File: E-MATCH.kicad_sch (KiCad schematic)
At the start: 7 parts, among them IC1 NCV81071BZR2G, J1 Screw_Terminal_01x02, Q1 IRF3205, U1 TMCS1108A2UQDR

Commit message: Updating Schematic Test
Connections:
- net 3V3 is gone; now on net 5V: U1.8 (VS)
- net Sensor_Output: now reaches U1.7 (VOUT)
- net Sensor_Output: now also A1.19 (A0)
- net 5V: now reaches A1.27 (+5V)
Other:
- moved on the sheet: D1
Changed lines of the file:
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@@
 	)
 	(junction
-		(at 45.72 102.87)
+		(at 45.72 85.09)
 		(diameter 0)
 		(color 0 0 0 0)
 	)
 	(junction
-		(at 45.72 88.9)
+		(at 45.72 95.25)
 		(diameter 0)
 		(color 0 0 0 0)
@@
 	(wire
 		(pts
-			(xy 45.72 102.87) (xy 45.72 119.38)
+			(xy 172.72 62.23) (xy 177.8 62.23)
+		)
+		(stroke
+			(width 0)
+			(type default)
+		)
+	)
+	(wire
+		(pts
+			(xy 45.72 91.44) (xy 45.72 95.25)
 		)
 		(stroke
@@
 	(wire
 		(pts
+			(xy 45.72 85.09) (xy 45.72 88.9)
+		)
+		(stroke
+			(width 0)
+			(type default)
+		)
+	)
+	(wire
+		(pts
 			(xy 95.25 60.96) (xy 95.25 67.31)
 		)
@@
 	(wire
 		(pts
-			(xy 45.72 88.9) (xy 45.72 59.69)
+			(xy 45.72 59.69) (xy 45.72 85.09)
 		)
 		(stroke
@@
 	(wire
 		(pts
+			(xy 165.1 35.56) (xy 165.1 36.83)
+		)
+		(stroke
+			(width 0)
+			(type default)
+		)
+	)
+	(wire
+		(pts
 			(xy 50.8 59.69) (xy 50.8 58.42)
 		)
@@
 	(wire
 		(pts
-			(xy 45.72 102.87) (xy 74.93 102.87)
-		)
-		(stroke
-			(width 0)
-			(type default)
-		)
-	)
-	(wire
-		(pts
-			(xy 74.93 88.9) (xy 74.93 93.98)
-		)
-		(stroke
-			(width 0)
-			(type default)
-		)
-	)
-	(wire
-		(pts
 			(xy 160.02 87.63) (xy 160.02 90.17)
 		)
@@
 	(wire
 		(pts
+			(xy 88.9 50.8) (xy 91.44 50.8)
+		)
+		(stroke
+			(width 0)
+			(type default)
+		)
+	)
+	(wire
+		(pts
+			(xy 45.72 95.25) (xy 45.72 119.38)
+		)
+		(stroke
+			(width 0)
+			(type default)
+		)
+	)
+	(wire
+		(pts
 			(xy 53.34 45.72) (xy 49.53 45.72)
 		)
@@
 	(wire
 		(pts
-			(xy 45.72 91.44) (xy 45.72 102.87)
-		)
-		(stroke
-			(width 0)
-			(type default)
-		)
-	)
-	(wire
-		(pts
 			(xy 45.72 46.99) (xy 49.53 46.99)
 		)
@@
 	(wire
 		(pts
-			(xy 45.72 88.9) (xy 74.93 88.9)
-		)
-		(stroke
-			(width 0)
-			(type default)
-		)
-	)
-	(wire
-		(pts
 			(xy 50.8 59.69) (xy 50.8 60.96)
 		)
@@
 	(wire
 		(pts
+			(xy 45.72 95.25) (xy 57.15 95.25)
+		)
+		(stroke
+			(width 0)
+			(type default)
+		)
+	)
+	(wire
+		(pts
 			(xy 140.97 128.27) (xy 148.59 128.27)
 		)
@@
 	(wire
 		(pts
-			(xy 74.93 102.87) (xy 74.93 104.14)
+			(xy 57.15 85.09) (xy 45.72 85.09)
 		)
 		(stroke
@@
 		)
 	)
-	(global_label "3V3"
+	(global_label "5V"
 		(shape input)
 		(at 93.98 45.72 0)
@@
 		)
 		(property "Intersheetrefs" "${INTERSHEET_REFS}"
-			(at 100.4728 45.72 0)
+			(at 99.2633 45.72 0)
+			(effects
+				(font
+					(size 1.27 1.27)
+				)
+				(justify left)
+				(hide yes)
+			)
+		)
+	)
+	(global_label "5V"
+		(shape input)
+		(at 165.1 35.56 90)
+		(fields_autoplaced yes)
+		(effects
+			(font
+				(size 1.27 1.27)
+			)
+			(justify left)
+		)
+		(property "Intersheetrefs" "${INTERSHEET_REFS}"
+			(at 165.1 30.2767 90)
+			(effects
+				(font
+					(size 1.27 1.27)
+				)
+				(justify left)
+				(hide yes)
+			)
+		)
+	)
+	(global_label "Sensor_Output"
+		(shape input)
+		(at 91.44 50.8 0)
+		(fields_autoplaced yes)
+		(effects
+			(font
+				(size 1.27 1.27)
+			)
+			(justify left)
+		)
+		(property "Intersheetrefs" "${INTERSHEET_REFS}"
+			(at 108.0321 50.8 0)
 			(effects
 				(font
@@
 		(property "Intersheetrefs" "${INTERSHEET_REFS}"
 			(at 53.12 36.83 0)
+			(effects
+				(font
+					(size 1.27 1.27)
+				)
+				(justify left)
+				(hide yes)
+			)
+		)
+	)
+	(global_label "Sensor_Output"
+		(shape input)
+		(at 177.8 62.23 0)
+		(fields_autoplaced yes)
+		(effects
+			(font
+				(size 1.27 1.27)
+			)
+			(justify left)
+		)
+		(property "Intersheetrefs" "${INTERSHEET_REFS}"
+			(at 194.3921 62.23 0)
 			(effects
 				(font
@@
 	(symbol
 		(lib_id "Schottky Diode:MBRS540T3G")
-		(at 74.93 99.06 90)
+		(at 57.15 90.17 90)
 		(unit 1)
 		(exclude_from_sim no)
@@
 		(fields_autoplaced yes)
 		(property "Reference" "D1"
-			(at 77.47 97.7899 90)
+			(at 59.69 88.8999 90)
 			(effects
 				(font
@@
 		)
 		(property "Value" "MBRS540T3G"
-			(at 77.47 100.3299 90)
+			(at 59.69 91.4399 90)
 			(effects
 				(font
@@
 		)
 		(property "Footprint" "Schottky Diode:DIOM7959X261N"
-			(at 74.93 99.06 0)
+			(at 57.15 90.17 0)
 			(effects
 				(font
@@
 		)
 		(property "Datasheet" ""
-			(at 74.93 99.06 0)
+			(at 57.15 90.17 0)
 			(effects
 				(font
@@
 		)
 		(property "Description" ""
-			(at 74.93 99.06 0)
+			(at 57.15 90.17 0)
 			(effects
 				(font
@@
 		)
 		(property "PARTREV" "7/27/2017"
-			(at 74.93 99.06 0)
+			(at 57.15 90.17 0)
 			(effects
 				(font
@@
 		)
 		(property "STANDARD" "IPC-7351B"
-			(at 74.93 99.06 0)
+			(at 57.15 90.17 0)
 			(effects
 				(font
@@
 		)
 		(property "MAXIMUM_PACKAGE_HEIGHT" "2.61 mm"
-			(at 74.93 99.06 0)
+			(at 57.15 90.17 0)
 			(effects
 				(font
@@
 		)
 		(property "MANUFACTURER" "ON SEMICONDUCTOR"
-			(at 74.93 99.06 0)
-			(effects
-				(font
+			(at 57.15 90.17 0)
+			(effects
+				(font

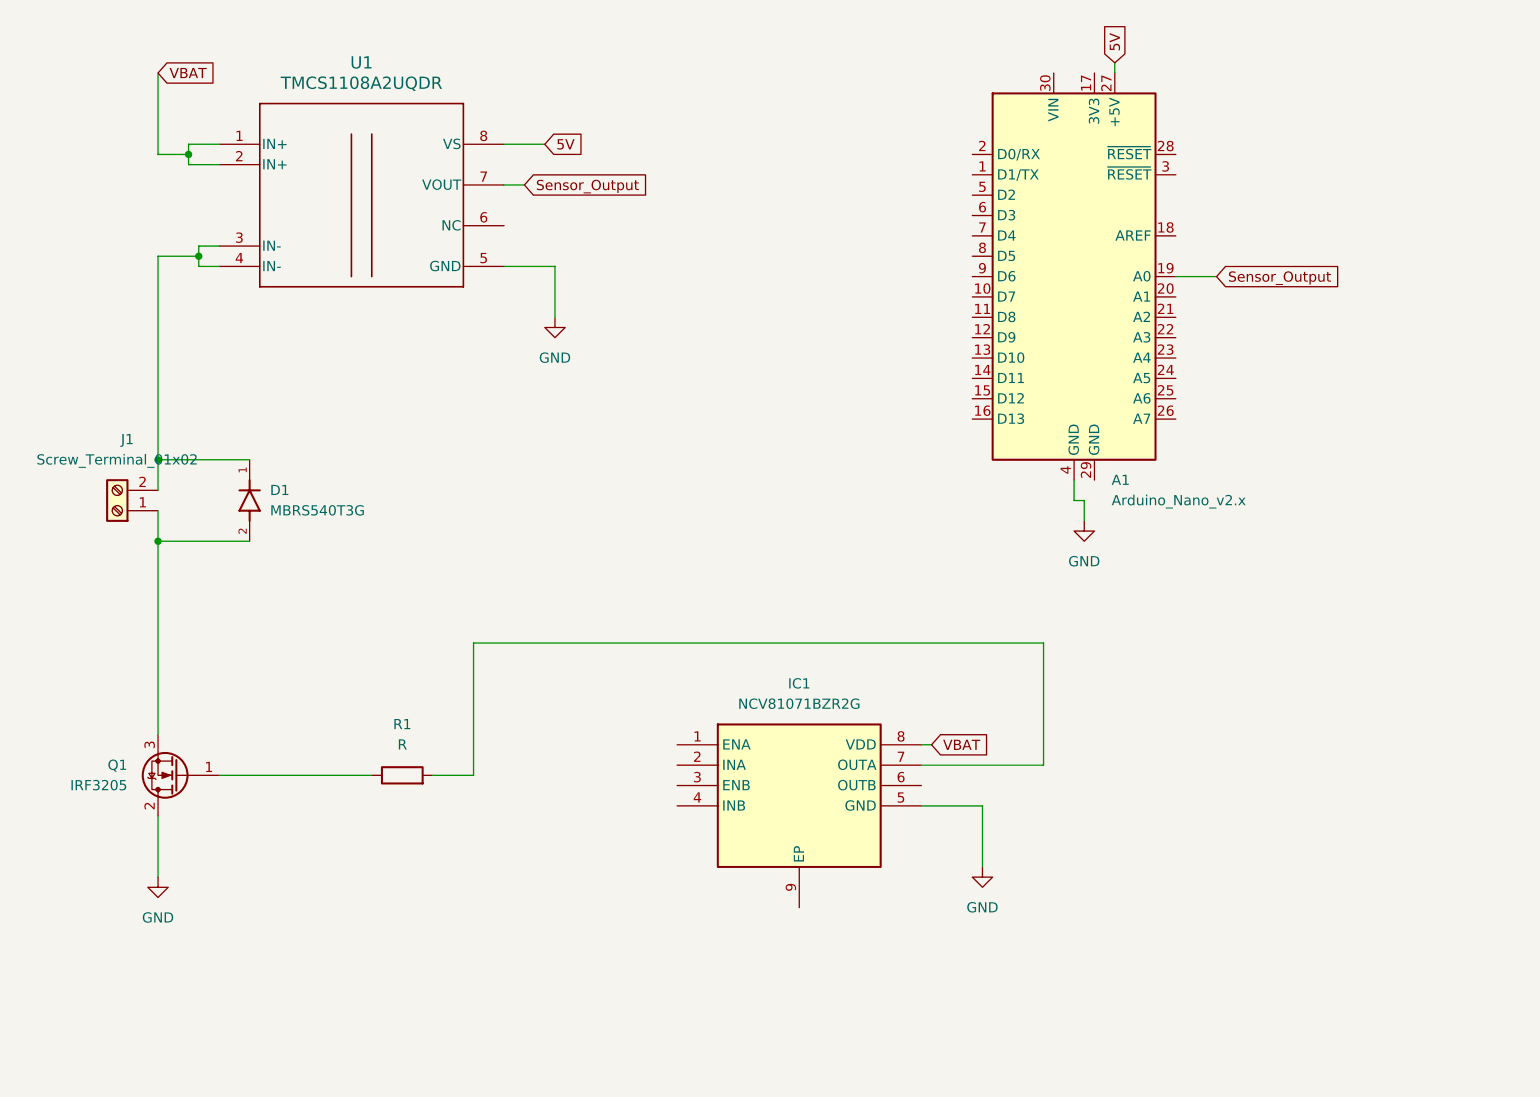
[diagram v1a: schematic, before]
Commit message: Resistor and Screw Terminal E-Cad Models were added!
Additionally, some progress was made in the schematic.
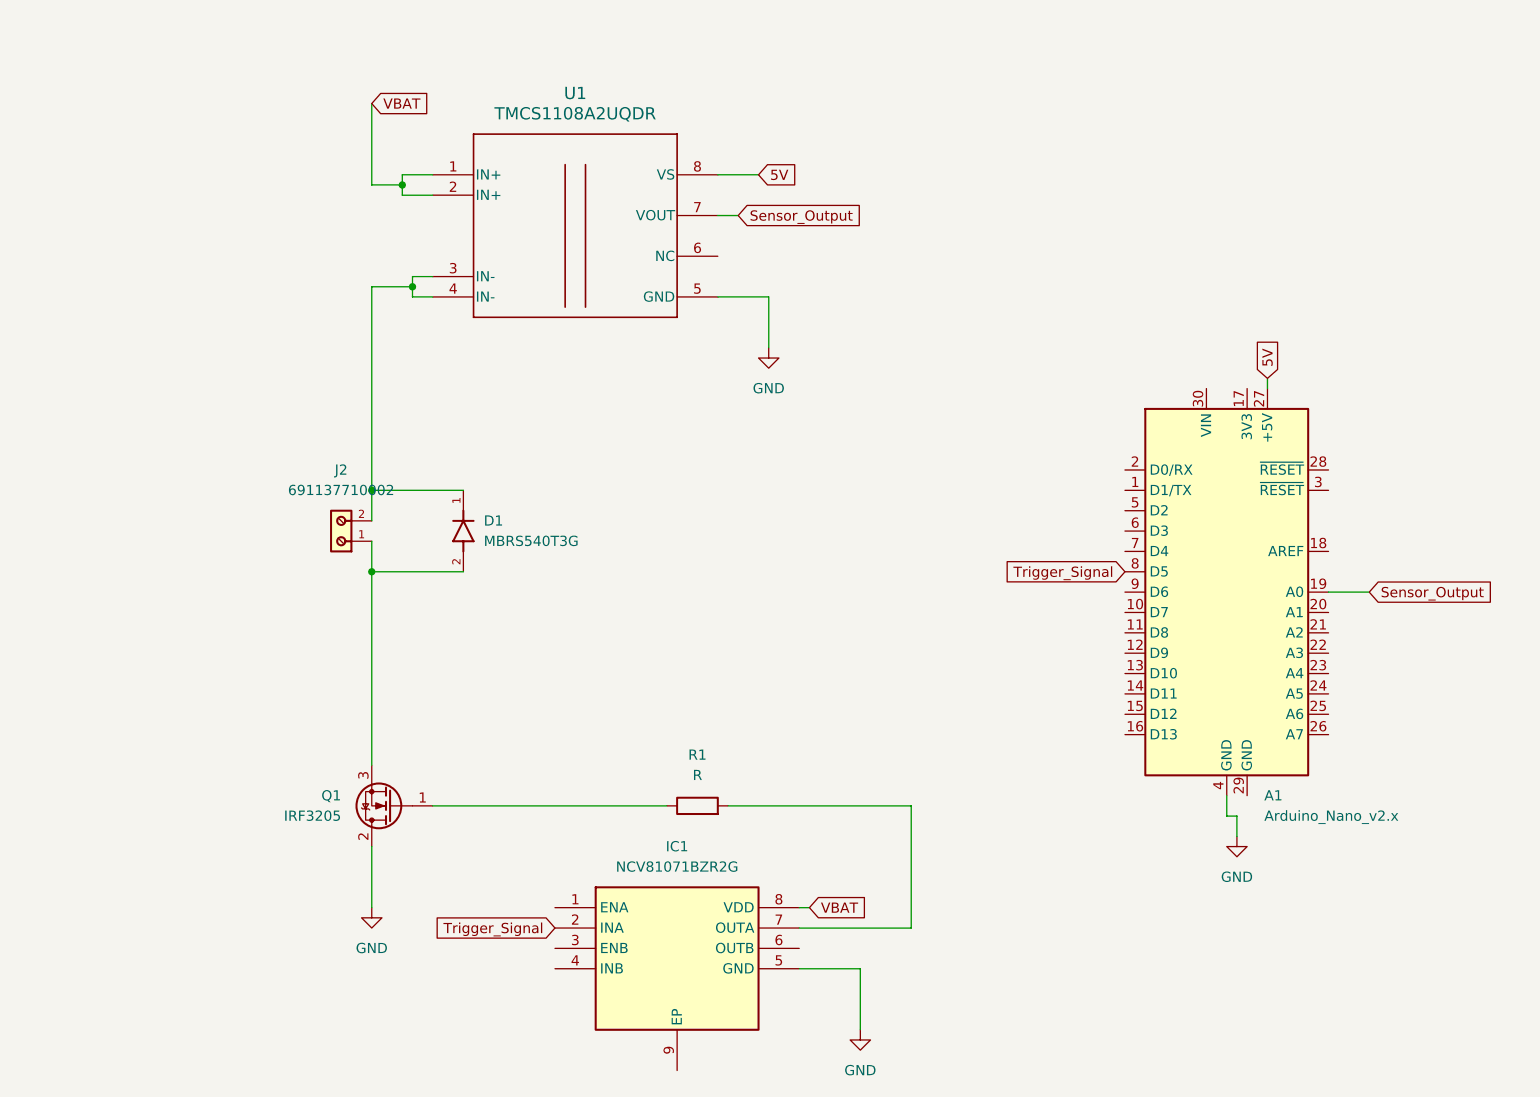
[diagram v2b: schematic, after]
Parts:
- removed J1: Screw_Terminal_01x02, symbol Connector:Screw_Terminal_01x02
- added J2: 691137710002, Screw_Terminal_0102:691137710002, symbol Screw Terminal:691137710002
- R1: footprint (none) -> Gate Resistor:RES_RC1206_YAG
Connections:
- net at D1.1, U1.3 (IN-), U1.4 (IN-): now also J2.2
- net at D1.2, Q1.3 (S): now also J2.1
- net Trigger_Signal: now reaches IC1.2 (INA)
- net Trigger_Signal: now also A1.8 (D5)
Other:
- moved on the sheet: A1, D1, IC1, Q1, R1, U1

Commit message: Added Text-Descriptions
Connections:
- net GND: now also IC1.3 (ENB), IC1.4 (INB)
- net Enable_Signal: now reaches IC1.1 (ENA)
- net Enable_Signal: now also A1.10 (D7)
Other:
- note added: "+Battery Voltage(7-8V)"
- note added: "Arduino Nano(Micro Controller)"
- note added: "Current Sensor"
- note added: "Drain"
- note added: "E-MATCH goes here"
- note added: "GATE DRIVER IC"
- note added: "Inputs"
- note added: "Mosfet Gate"
- note added: "No connect"
- note added: "Outputs"
- note added: "Resistor to limit gate driving current to around 1 Ampere"
- note added: "SCHOTTCKY DIODE"
- note added: "Source"
- moved on the sheet: A1

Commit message: Neat placement for schematic
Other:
- note added: "CURRENT SENSOR"
- note removed: "Current Sensor"
- moved on the sheet: A1, D1, IC1, J2, Q1, R1, U1

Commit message: New Diode- smaller footprint
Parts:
- removed D1: MBRS540T3G, Schottky Diode:DIOM7959X261N, symbol Schottky Diode:MBRS540T3G
- added CR1: MSS1P5-M3/89A, DIODE_MSP3V3, symbol Schottcky Diode:MSS1P5-M3_89A
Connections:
- net at J2.2, U1.3 (IN-), U1.4 (IN-): now also CR1.1
- net at J2.1, Q1.3 (S): now also CR1.2
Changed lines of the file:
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@@
-	)
-	(symbol
-		(lib_id "Schottky Diode:MBRS540T3G")
-		(at 58.42 93.98 90)
-		(unit 1)
-		(exclude_from_sim no)
-		(in_bom yes)
-		(on_board yes)
-		(dnp no)
-		(fields_autoplaced yes)
-		(property "Reference" "D1"
-			(at 60.96 92.7099 90)
-			(effects
-				(font
-					(size 1.27 1.27)
-				)
-				(justify right)
-			)
-		)
-		(property "Value" "MBRS540T3G"
-			(at 60.96 95.2499 90)
-			(effects
-				(font
-					(size 1.27 1.27)
-				)
-				(justify right)
-			)
-		)
-		(property "Footprint" "Schottky Diode:DIOM7959X261N"
-			(at 58.42 93.98 0)
-			(effects
-				(font
-					(size 1.27 1.27)
-				)
-				(justify bottom)
-				(hide yes)
-			)
-		)
-		(property "Datasheet" ""
-			(at 58.42 93.98 0)
-			(effects
-				(font
-					(size 1.27 1.27)
-				)
-				(hide yes)
-			)
-		)
-		(property "Description" ""
-			(at 58.42 93.98 0)
-			(effects
-				(font
-					(size 1.27 1.27)
-				)
-				(hide yes)
-			)
-		)
-		(property "PARTREV" "7/27/2017"
-			(at 58.42 93.98 0)
-			(effects
-				(font
-					(size 1.27 1.27)
-				)
-				(justify bottom)
-				(hide yes)
-			)
-		)
-		(property "STANDARD" "IPC-7351B"
-			(at 58.42 93.98 0)
-			(effects
-				(font
-					(size 1.27 1.27)
-				)
-				(justify bottom)
-				(hide yes)
-			)
-		)
-		(property "MAXIMUM_PACKAGE_HEIGHT" "2.61 mm"
-			(at 58.42 93.98 0)
-			(effects
-				(font
-					(size 1.27 1.27)
-				)
-				(justify bottom)
-				(hide yes)
-			)
-		)
-		(property "MANUFACTURER" "ON SEMICONDUCTOR"
-			(at 58.42 93.98 0)
-			(effects
-				(font
-					(size 1.27 1.27)
-				)
-				(justify bottom)
-				(hide yes)
-			)
-		)
-		(pin "1"
-		)
-		(pin "2"
-		)
-		(instances
-			(project ""
-				(path "/ac49d8b8-9946-4b6b-9646-a2b20606c52a"
-					(reference "D1")
-					(unit 1)
-				)
-			)
-		)
 	)
 	(symbol
@@
 					(unit 1)
 				)
+			)
+		)
+	)
+	(symbol
+		(lib_id "Schottcky Diode:MSS1P5-M3_89A")
+		(at 58.42 99.06 90)
+		(unit 1)
+		(exclude_from_sim no)
+		(in_bom yes)
+		(on_board yes)
+		(dnp no)
+		(fields_autoplaced yes)
+		(property "Reference" "CR1"
+			(at 62.23 92.7099 90)
+			(effects
+				(font
+					(size 1.524 1.524)
+				)
+				(justify right)
+			)
+		)
+		(property "Value" "MSS1P5-M3/89A"
+			(at 62.23 95.2499 90)
+			(effects
+				(font
+					(size 1.524 1.524)
+				)
+				(justify right)
+			)
+		)
+		(property "Footprint" "DIODE_MSP3V3"
+			(at 58.42 99.06 0)
+			(effects
+				(font
+					(size 1.27 1.27)
+					(italic yes)
+				)
+				(hide yes)
+			)
+		)
+		(property "Datasheet" "https://www.vishay.com/doc?89018"
+			(at 58.42 99.06 0)
+			(effects
+				(font
+					(size 1.27 1.27)
+					(italic yes)
+				)
+				(hide yes)
+			)
+		)
+		(property "Description" ""
+			(at 58.42 99.06 0)
+			(effects
+				(font
+					(size 1.27 1.27)
+				)
+				(hide yes)
+			)
+		)
+		(pin "1"
+		)
+		(pin "2"
+		)
+		(instances
+			(project ""
+				(path "/ac49d8b8-9946-4b6b-9646-a2b20606c52a"
+					(reference "CR1")
+					(unit 1)
+				)

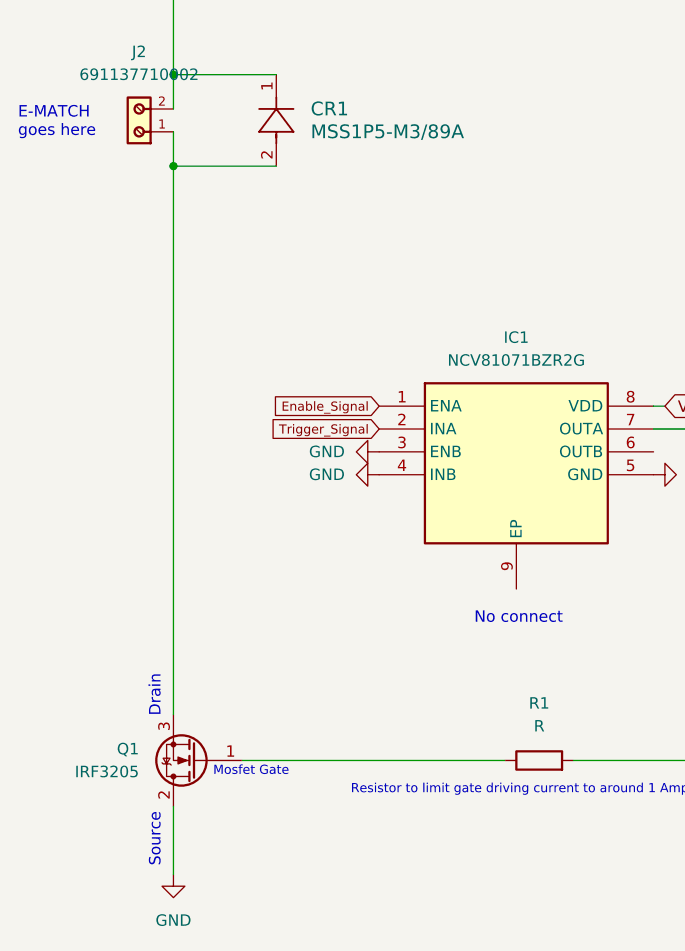
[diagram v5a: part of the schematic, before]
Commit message: New Mosfet plus linked some 3-d models
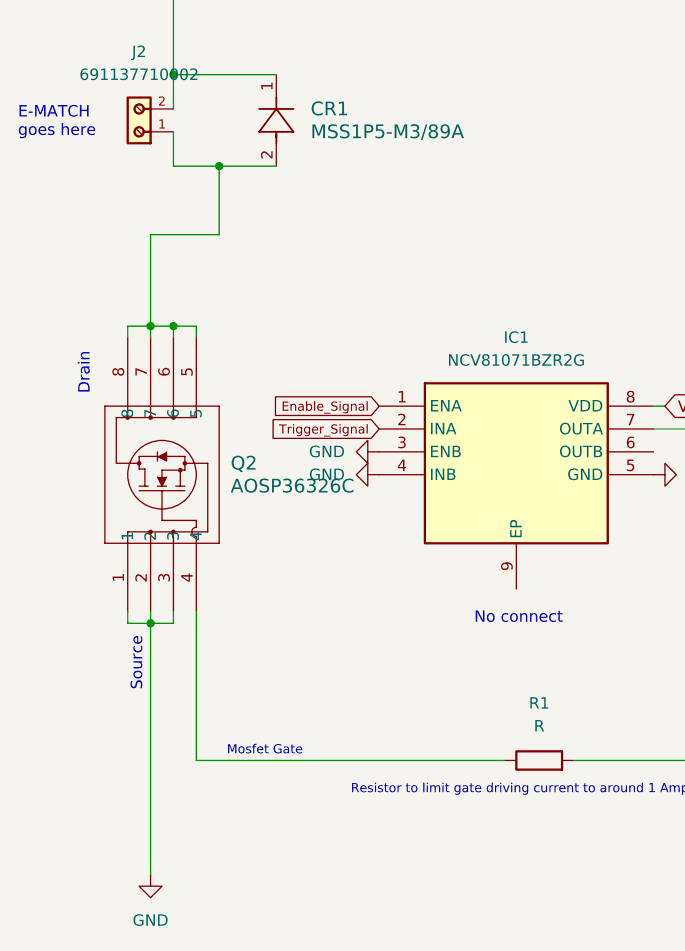
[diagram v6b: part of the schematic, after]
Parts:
- removed Q1: IRF3205, Package_TO_SOT_THT:TO-220-3_Vertical, symbol Transistor_FET:IRF3205
- added Q2: AOSP36326C, SO8SOP-8L_AOS, symbol N-Ch Mosfet:AOSP36326C
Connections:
- net GND: now also Q2.1, Q2.2, Q2.3
- net at CR1.2, J2.1: now also Q2.5, Q2.6, Q2.7, Q2.8
- net at R1.1: now also Q2.4
